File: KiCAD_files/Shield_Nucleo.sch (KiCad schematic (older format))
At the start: 53 parts, among them J1 Shield_nucleo_stage_outline, J2 RJ45, J3 RJ45, U1 NUCLEO-F401RE, U2 AT25xxx, U3 TCAN334

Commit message: Work in progress- shield V1.0
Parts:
- TP1, TP10, TP11, TP12, TP13, TP14, TP15, TP16, TP17, TP18, TP19, TP2, TP20, TP21, TP22, TP23, TP24, TP25, TP26, TP27, TP28, TP29, TP3, TP30, TP4, TP5, TP6, TP7, TP8, TP9: footprint TestPoint:TestPoint_Plated_Hole_D2.0mm -> TestPoint:TestPoint_THTPad_D2.5mm_Drill1.2mm
- U1: footprint Footprints:ST_NUCLEO-F401RE_modified -> Footprints:ST_NUCLEO-G474
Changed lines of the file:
@@
 F 0 "U1" H 2150 4967 50  0000 C CNN
 F 1 "NUCLEO-F401RE" H 2150 4876 50  0000 C CNN
-F 2 "Footprints:ST_NUCLEO-F401RE_modified" H 2150 3200 50  0001 L BNN
+F 2 "Footprints:ST_NUCLEO-G474" H 2150 3200 50  0001 L BNN
 F 3 "Manufacturer Recommendations" H 2150 3200 50  0001 L BNN
 F 4 "13" H 2150 3200 50  0001 L BNN "Field4"
@@
 F 0 "U1" H 5800 4917 50  0000 C CNN
 F 1 "NUCLEO-F401RE" H 5800 4826 50  0000 C CNN
-F 2 "Footprints:ST_NUCLEO-F401RE_modified" H 5800 3250 50  0001 L BNN
+F 2 "Footprints:ST_NUCLEO-G474" H 5800 3250 50  0001 L BNN
 F 3 "Manufacturer Recommendations" H 5800 3250 50  0001 L BNN
 F 4 "13" H 5800 3250 50  0001 L BNN "Field4"
@@
 Wire Wire Line
 	3050 4800 2950 4800
-Text Label 11350 2800 0    50   ~ 0
-AGND
 Text Label 11350 3050 0    50   ~ 0
 AGND
@@
 	11350 3050 11100 3050
 Wire Wire Line
-	11350 2800 11100 2800
-Wire Wire Line
 	11350 3550 11100 3550
 Wire Wire Line
@@
 F 0 "TP22" V 8650 3050 50  0000 L CNN
 F 1 "TestPoint" V 8650 3250 50  0001 L CNN
-F 2 "TestPoint:TestPoint_Plated_Hole_D2.0mm" H 8850 2800 50  0001 C CNN
+F 2 "TestPoint:TestPoint_THTPad_D2.5mm_Drill1.2mm" H 8850 2800 50  0001 C CNN
 F 3 "~" H 8850 2800 50  0001 C CNN
 	1    8650 2800
@@
 F 0 "TP21" V 8650 2950 50  0000 L CNN
 F 1 "TestPoint" V 8650 3150 50  0001 L CNN
-F 2 "TestPoint:TestPoint_Plated_Hole_D2.0mm" H 8850 2700 50  0001 C CNN
+F 2 "TestPoint:TestPoint_THTPad_D2.5mm_Drill1.2mm" H 8850 2700 50  0001 C CNN
 F 3 "~" H 8850 2700 50  0001 C CNN
 	1    8650 2700
@@
 F 0 "TP24" V 8650 3300 50  0000 L CNN
 F 1 "TestPoint" V 8650 3500 50  0001 L CNN
-F 2 "TestPoint:TestPoint_Plated_Hole_D2.0mm" H 8850 3050 50  0001 C CNN
+F 2 "TestPoint:TestPoint_THTPad_D2.5mm_Drill1.2mm" H 8850 3050 50  0001 C CNN
 F 3 "~" H 8850 3050 50  0001 C CNN
 	1    8650 3050
@@
 F 0 "TP23" V 8650 3200 50  0000 L CNN
 F 1 "TestPoint" V 8650 3400 50  0001 L CNN
-F 2 "TestPoint:TestPoint_Plated_Hole_D2.0mm" H 8850 2950 50  0001 C CNN
+F 2 "TestPoint:TestPoint_THTPad_D2.5mm_Drill1.2mm" H 8850 2950 50  0001 C CNN
 F 3 "~" H 8850 2950 50  0001 C CNN
 	1    8650 2950
@@
 F 0 "TP26" V 8650 3550 50  0000 L CNN
 F 1 "TestPoint" V 8650 3750 50  0001 L CNN
-F 2 "TestPoint:TestPoint_Plated_Hole_D2.0mm" H 8850 3300 50  0001 C CNN
+F 2 "TestPoint:TestPoint_THTPad_D2.5mm_Drill1.2mm" H 8850 3300 50  0001 C CNN
 F 3 "~" H 8850 3300 50  0001 C CNN
 	1    8650 3300
@@
 F 0 "TP25" V 8650 3450 50  0000 L CNN
 F 1 "TestPoint" V 8650 3650 50  0001 L CNN
-F 2 "TestPoint:TestPoint_Plated_Hole_D2.0mm" H 8850 3200 50  0001 C CNN
+F 2 "TestPoint:TestPoint_THTPad_D2.5mm_Drill1.2mm" H 8850 3200 50  0001 C CNN
 F 3 "~" H 8850 3200 50  0001 C CNN
 	1    8650 3200
@@
 F 0 "TP17" V 7050 2600 50  0000 L CNN
 F 1 "TestPoint" V 7050 2800 50  0001 L CNN
-F 2 "TestPoint:TestPoint_Plated_Hole_D2.0mm" H 7250 2350 50  0001 C CNN
+F 2 "TestPoint:TestPoint_THTPad_D2.5mm_Drill1.2mm" H 7250 2350 50  0001 C CNN
 F 3 "~" H 7250 2350 50  0001 C CNN
 	1    7050 2350
@@
 F 0 "TP18" V 7050 2700 50  0000 L CNN
 F 1 "TestPoint" V 7050 2900 50  0001 L CNN
-F 2 "TestPoint:TestPoint_Plated_Hole_D2.0mm" H 7250 2450 50  0001 C CNN
+F 2 "TestPoint:TestPoint_THTPad_D2.5mm_Drill1.2mm" H 7250 2450 50  0001 C CNN
 F 3 "~" H 7250 2450 50  0001 C CNN
 	1    7050 2450
@@
 F 0 "TP19" V 7050 2800 50  0000 L CNN
 F 1 "TestPoint" V 7050 3000 50  0001 L CNN
-F 2 "TestPoint:TestPoint_Plated_Hole_D2.0mm" H 7250 2550 50  0001 C CNN
+F 2 "TestPoint:TestPoint_THTPad_D2.5mm_Drill1.2mm" H 7250 2550 50  0001 C CNN
 F 3 "~" H 7250 2550 50  0001 C CNN
 	1    7050 2550
@@
 F 0 "TP20" V 7050 2900 50  0000 L CNN
 F 1 "TestPoint" V 7050 3100 50  0001 L CNN
-F 2 "TestPoint:TestPoint_Plated_Hole_D2.0mm" H 7250 2650 50  0001 C CNN
+F 2 "TestPoint:TestPoint_THTPad_D2.5mm_Drill1.2mm" H 7250 2650 50  0001 C CNN
 F 3 "~" H 7250 2650 50  0001 C CNN
 	1    7050 2650
@@
 F 0 "TP5" V 4550 3000 50  0000 L CNN
 F 1 "TestPoint" V 4550 3200 50  0001 L CNN
-F 2 "TestPoint:TestPoint_Plated_Hole_D2.0mm" H 4750 2750 50  0001 C CNN
+F 2 "TestPoint:TestPoint_THTPad_D2.5mm_Drill1.2mm" H 4750 2750 50  0001 C CNN
 F 3 "~" H 4750 2750 50  0001 C CNN
 	1    4550 2750
@@
 F 0 "TP4" V 4550 2900 50  0000 L CNN
 F 1 "TestPoint" V 4550 3100 50  0001 L CNN
-F 2 "TestPoint:TestPoint_Plated_Hole_D2.0mm" H 4750 2650 50  0001 C CNN
+F 2 "TestPoint:TestPoint_THTPad_D2.5mm_Drill1.2mm" H 4750 2650 50  0001 C CNN
 F 3 "~" H 4750 2650 50  0001 C CNN
 	1    4550 2650
@@
 F 0 "TP7" V 4550 3200 50  0000 L CNN
 F 1 "TestPoint" V 4550 3400 50  0001 L CNN
-F 2 "TestPoint:TestPoint_Plated_Hole_D2.0mm" H 4750 2950 50  0001 C CNN
+F 2 "TestPoint:TestPoint_THTPad_D2.5mm_Drill1.2mm" H 4750 2950 50  0001 C CNN
 F 3 "~" H 4750 2950 50  0001 C CNN
 	1    4550 2950
@@
 F 0 "TP6" V 4550 3100 50  0000 L CNN
 F 1 "TestPoint" V 4550 3300 50  0001 L CNN
-F 2 "TestPoint:TestPoint_Plated_Hole_D2.0mm" H 4750 2850 50  0001 C CNN
+F 2 "TestPoint:TestPoint_THTPad_D2.5mm_Drill1.2mm" H 4750 2850 50  0001 C CNN
 F 3 "~" H 4750 2850 50  0001 C CNN
 	1    4550 2850
@@
 F 0 "TP9" V 4550 4600 50  0000 L CNN
 F 1 "TestPoint" V 4550 4800 50  0001 L CNN
-F 2 "TestPoint:TestPoint_Plated_Hole_D2.0mm" H 4750 4350 50  0001 C CNN
+F 2 "TestPoint:TestPoint_THTPad_D2.5mm_Drill1.2mm" H 4750 4350 50  0001 C CNN
 F 3 "~" H 4750 4350 50  0001 C CNN
 	1    4550 4350
@@
 F 0 "TP8" V 4550 4500 50  0000 L CNN
 F 1 "TestPoint" V 4550 4700 50  0001 L CNN
-F 2 "TestPoint:TestPoint_Plated_Hole_D2.0mm" H 4750 4250 50  0001 C CNN
+F 2 "TestPoint:TestPoint_THTPad_D2.5mm_Drill1.2mm" H 4750 4250 50  0001 C CNN
 F 3 "~" H 4750 4250 50  0001 C CNN
 	1    4550 4250
@@
 F 0 "TP11" V 4550 4800 50  0000 L CNN
 F 1 "TestPoint" V 4550 5000 50  0001 L CNN
-F 2 "TestPoint:TestPoint_Plated_Hole_D2.0mm" H 4750 4550 50  0001 C CNN
+F 2 "TestPoint:TestPoint_THTPad_D2.5mm_Drill1.2mm" H 4750 4550 50  0001 C CNN
 F 3 "~" H 4750 4550 50  0001 C CNN
 	1    4550 4550
@@
 F 0 "TP10" V 4550 4700 50  0000 L CNN
 F 1 "TestPoint" V 4550 4900 50  0001 L CNN
-F 2 "TestPoint:TestPoint_Plated_Hole_D2.0mm" H 4750 4450 50  0001 C CNN
+F 2 "TestPoint:TestPoint_THTPad_D2.5mm_Drill1.2mm" H 4750 4450 50  0001 C CNN
 F 3 "~" H 4750 4450 50  0001 C CNN
 	1    4550 4450
@@
 F 0 "TP13" H 6600 9050 50  0000 L CNN
 F 1 "TestPoint" V 6550 9450 50  0001 L CNN
-F 2 "TestPoint:TestPoint_Plated_Hole_D2.0mm" H 6750 9000 50  0001 C CNN
+F 2 "TestPoint:TestPoint_THTPad_D2.5mm_Drill1.2mm" H 6750 9000 50  0001 C CNN
 F 3 "~" H 6750 9000 50  0001 C CNN
 	1    6550 9000
@@
 F 0 "TP14" H 6600 9350 50  0000 L CNN
 F 1 "TestPoint" V 6550 9750 50  0001 L CNN
-F 2 "TestPoint:TestPoint_Plated_Hole_D2.0mm" H 6750 9300 50  0001 C CNN
+F 2 "TestPoint:TestPoint_THTPad_D2.5mm_Drill1.2mm" H 6750 9300 50  0001 C CNN
 F 3 "~" H 6750 9300 50  0001 C CNN
 	1    6550 9300
@@
 F 0 "TP15" H 6600 9700 50  0000 L CNN
 F 1 "TestPoint" V 6550 10100 50  0001 L CNN
-F 2 "TestPoint:TestPoint_Plated_Hole_D2.0mm" H 6750 9650 50  0001 C CNN
+F 2 "TestPoint:TestPoint_THTPad_D2.5mm_Drill1.2mm" H 6750 9650 50  0001 C CNN
 F 3 "~" H 6750 9650 50  0001 C CNN
 	1    6550 9650
@@
 F 0 "TP16" H 6850 9850 50  0000 L CNN
 F 1 "TestPoint" V 6800 10250 50  0001 L CNN
-F 2 "TestPoint:TestPoint_Plated_Hole_D2.0mm" H 7000 9800 50  0001 C CNN
+F 2 "TestPoint:TestPoint_THTPad_D2.5mm_Drill1.2mm" H 7000 9800 50  0001 C CNN
 F 3 "~" H 7000 9800 50  0001 C CNN
 	1    6800 9800
@@
 F 0 "TP2" H 3050 1500 50  0000 L CNN
 F 1 "TestPoint" V 3000 1900 50  0001 L CNN
-F 2 "TestPoint:TestPoint_Plated_Hole_D2.0mm" H 3200 1450 50  0001 C CNN
+F 2 "TestPoint:TestPoint_THTPad_D2.5mm_Drill1.2mm" H 3200 1450 50  0001 C CNN
 F 3 "~" H 3200 1450 50  0001 C CNN
 	1    3000 1450
@@
 F 0 "TP1" H 1600 5200 50  0000 L CNN
 F 1 "TestPoint" V 1550 5600 50  0001 L CNN
-F 2 "TestPoint:TestPoint_Plated_Hole_D2.0mm" H 1750 5150 50  0001 C CNN
+F 2 "TestPoint:TestPoint_THTPad_D2.5mm_Drill1.2mm" H 1750 5150 50  0001 C CNN
 F 3 "~" H 1750 5150 50  0001 C CNN
 	1    1550 5150
@@
 F 0 "TP12" H 5000 5200 50  0000 L CNN
 F 1 "TestPoint" V 4950 5600 50  0001 L CNN
-F 2 "TestPoint:TestPoint_Plated_Hole_D2.0mm" H 5150 5150 50  0001 C CNN
+F 2 "TestPoint:TestPoint_THTPad_D2.5mm_Drill1.2mm" H 5150 5150 50  0001 C CNN
 F 3 "~" H 5150 5150 50  0001 C CNN
 	1    4950 5150
@@
 F 0 "TP3" H 3450 1950 50  0000 L CNN
 F 1 "TestPoint" V 3400 2350 50  0001 L CNN
-F 2 "TestPoint:TestPoint_Plated_Hole_D2.0mm" H 3600 1900 50  0001 C CNN
+F 2 "TestPoint:TestPoint_THTPad_D2.5mm_Drill1.2mm" H 3600 1900 50  0001 C CNN
 F 3 "~" H 3600 1900 50  0001 C CNN
 	1    3400 1900
@@
 F 0 "TP27" V 12300 2550 50  0000 L CNN
 F 1 "TestPoint" V 12400 2900 50  0001 L CNN
-F 2 "TestPoint:TestPoint_Plated_Hole_D2.0mm" H 12600 2450 50  0001 C CNN
+F 2 "TestPoint:TestPoint_THTPad_D2.5mm_Drill1.2mm" H 12600 2450 50  0001 C CNN
 F 3 "~" H 12600 2450 50  0001 C CNN
 	1    12400 2450
@@
 F 0 "TP28" V 13300 2800 50  0000 L CNN
 F 1 "TestPoint" V 13400 3150 50  0001 L CNN
-F 2 "TestPoint:TestPoint_Plated_Hole_D2.0mm" H 13600 2700 50  0001 C CNN
+F 2 "TestPoint:TestPoint_THTPad_D2.5mm_Drill1.2mm" H 13600 2700 50  0001 C CNN
 F 3 "~" H 13600 2700 50  0001 C CNN
 	1    13400 2700
@@
 F 0 "TP29" V 14150 3050 50  0000 L CNN
 F 1 "TestPoint" V 14250 3400 50  0001 L CNN
-F 2 "TestPoint:TestPoint_Plated_Hole_D2.0mm" H 14450 2950 50  0001 C CNN
+F 2 "TestPoint:TestPoint_THTPad_D2.5mm_Drill1.2mm" H 14450 2950 50  0001 C CNN
 F 3 "~" H 14450 2950 50  0001 C CNN
 	1    14250 2950
@@
 F 0 "TP30" V 15150 3250 50  0000 L CNN
 F 1 "TestPoint" V 15250 3600 50  0001 L CNN
-F 2 "TestPoint:TestPoint_Plated_Hole_D2.0mm" H 15450 3150 50  0001 C CNN
+F 2 "TestPoint:TestPoint_THTPad_D2.5mm_Drill1.2mm" H 15450 3150 50  0001 C CNN
 F 3 "~" H 15450 3150 50  0001 C CNN
 	1    15250 3150
@@
 Text Label 11300 2550 0    50   ~ 0
 E5V
+Wire Wire Line
+	11350 2800 11100 2800
+Text Label 11350 2800 0    50   ~ 0
+AGND
 $EndSCHEMATC

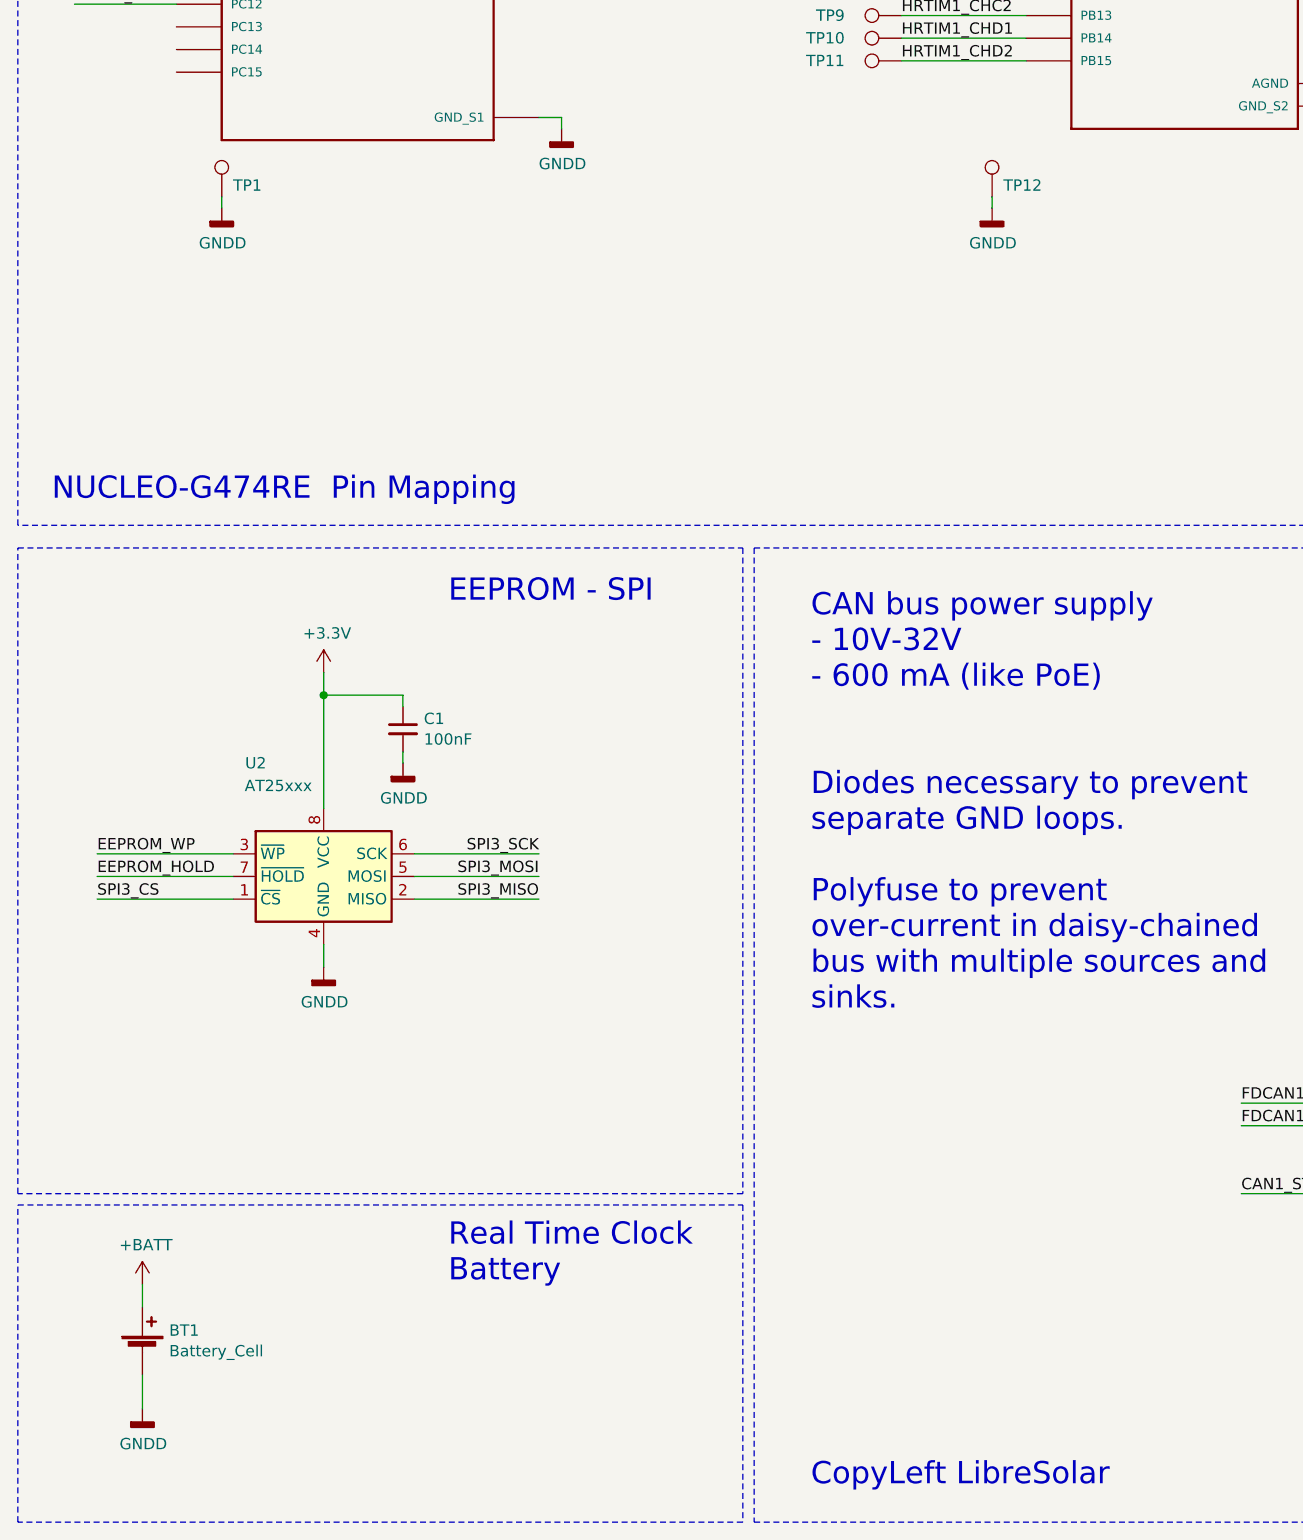
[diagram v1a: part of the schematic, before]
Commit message: Added missing 3Dfootprints
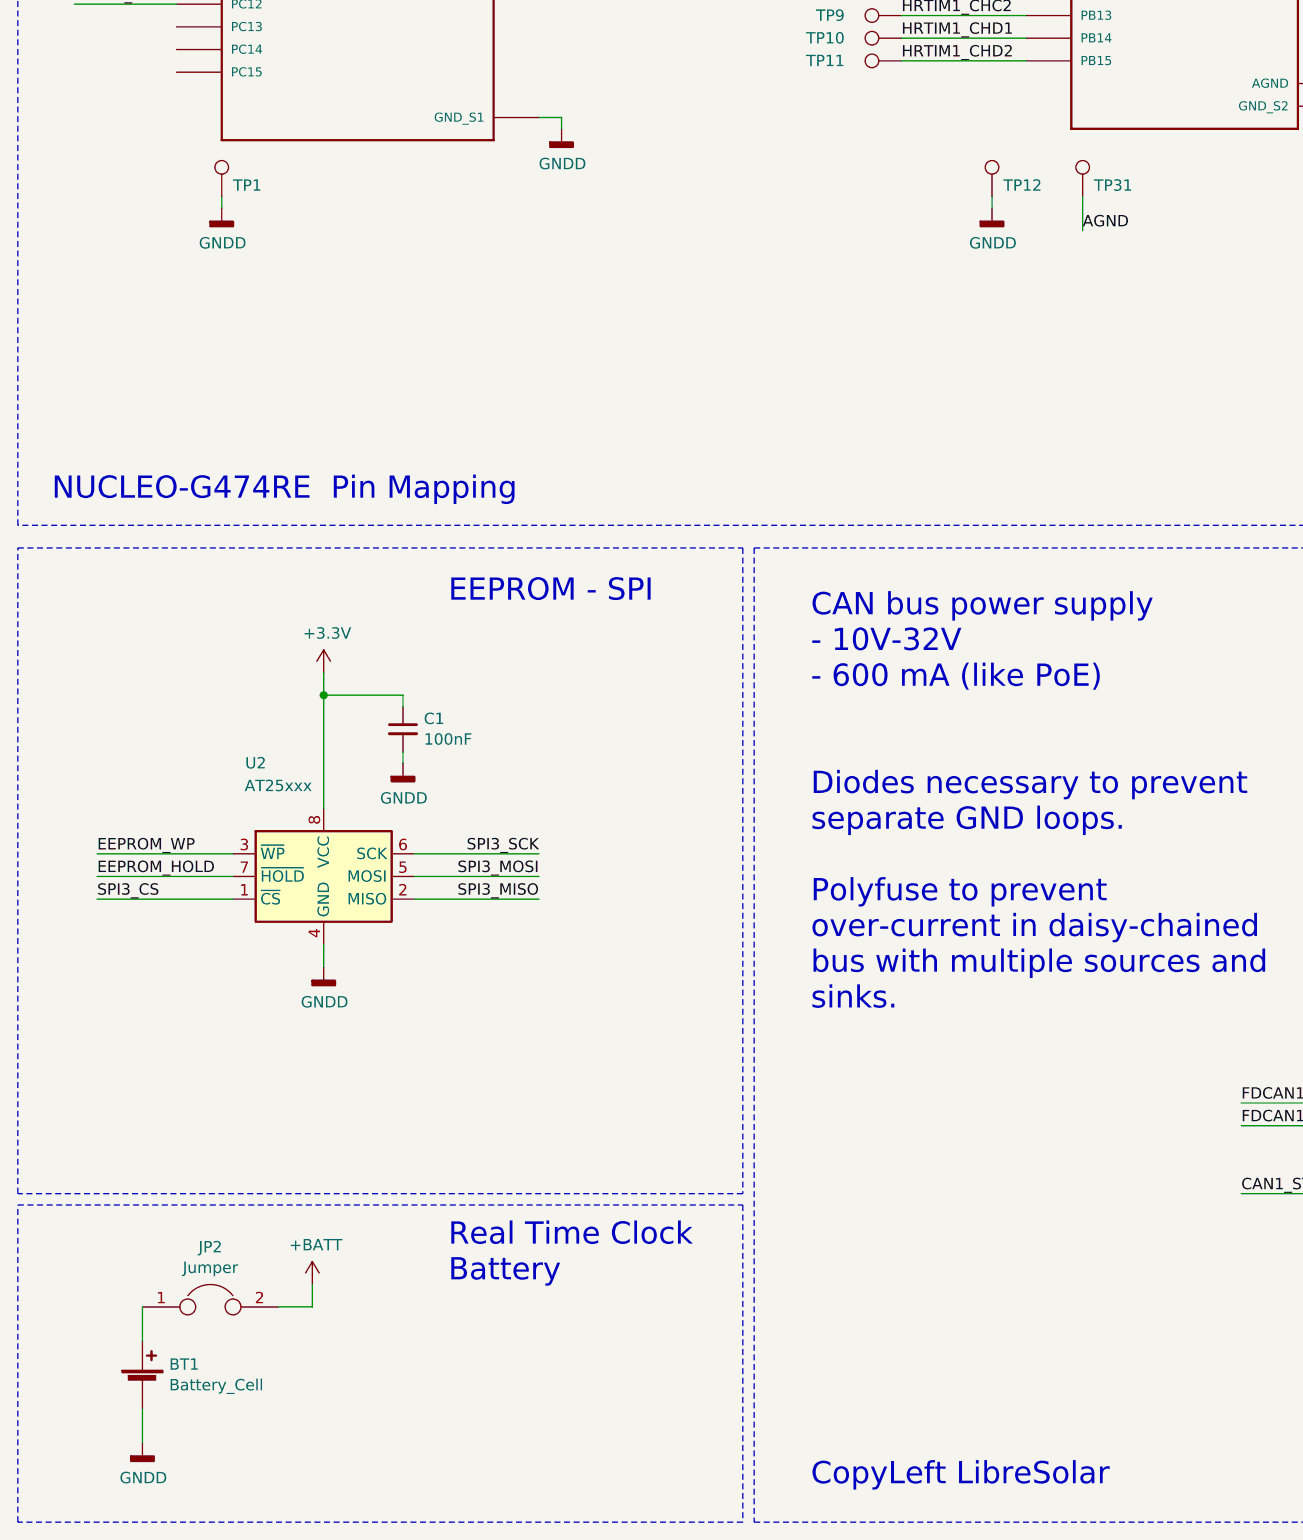
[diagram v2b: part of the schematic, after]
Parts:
- added JP2: Jumper, Connector_PinHeader_2.54mm:PinHeader_1x02_P2.54mm_Vertical, symbol Device:Jumper
- added TP31: TestPoint, TestPoint:TestPoint_THTPad_D2.5mm_Drill1.2mm, symbol Connector:TestPoint
- BT1: footprint TestPoint:TestPoint_Keystone_5010-5014_Multipurpose -> Footprints:CR2032
- U2, U3: footprint Package_SO:SO-8_3.9x4.9mm_P1.27mm -> Footprints:SOIC-8_3.9x4.9mm_P1.27mm
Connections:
- net +BATT: now also JP2.2; no longer BT1.1 (+)
- net AGND: now also TP31.1
- new net: BT1.1 (+), JP2.1
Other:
- moved on the sheet: BT1
